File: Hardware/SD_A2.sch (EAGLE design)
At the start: 25 parts, among them IC1 74LS245N, IC2 LM317, IC4 XC9572XL, IC5 28C64ASO

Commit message: Schematic as Eagle V7 file
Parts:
- C2: device rcl:CPOL-EU153CLV-0405 -> rcl@1:CPOL-EU153CLV-0405
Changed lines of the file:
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@@
 <part name="ST1" library="con-apple2" deviceset="A2-50PIN" device="SLOT1-3"/>
 <part name="IC4" library="xilinx-xc9" deviceset="XC9572_S44" device="" value="XC9572XL"/>
-<part name="IC1" library="74xx-eu" library_urn="urn:adsk.eagle:library:85" deviceset="74*245" device="N" technology="LS" value="74LS245N"/>
+<part name="IC1" library="74xx-eu" deviceset="74*245" device="N" technology="LS" value="74LS245N"/>
 <part name="IC2" library="v-reg" deviceset="LM317TL" device="" value="LM317"/>
-<part name="C2" library="rcl" library_urn="urn:adsk.eagle:library:334" deviceset="CPOL-EU" device="153CLV-0405" value="1u"/>
+<part name="C2" library="rcl@1" deviceset="CPOL-EU" device="153CLV-0405" value="1u"/>
 <part name="R1" library="rcl" deviceset="R-EU_" device="R0603" value="200"/>
 <part name="R2" library="rcl" deviceset="R-EU_" device="R0603" value="330"/>
@@
 <part name="GND9" library="supply1" deviceset="GND" device=""/>
 <part name="C1" library="rcl" deviceset="C-EU" device="C0603K" value="100n"/>
-<part name="P+6" library="supply1" library_urn="urn:adsk.eagle:library:371" deviceset="+12V" device=""/>
-<part name="P-1" library="supply1" library_urn="urn:adsk.eagle:library:371" deviceset="-5V" device=""/>
-<part name="P-2" library="supply1" library_urn="urn:adsk.eagle:library:371" deviceset="-12V" device=""/>
-<part name="P+7" library="supply1" library_urn="urn:adsk.eagle:library:371" deviceset="+12V" device=""/>
-<part name="P-3" library="supply1" library_urn="urn:adsk.eagle:library:371" deviceset="-12V" device=""/>
-<part name="P-4" library="supply1" library_urn="urn:adsk.eagle:library:371" deviceset="-5V" device=""/>
+<part name="P+6" library="supply1@1" deviceset="+12V" device=""/>
+<part name="P-1" library="supply1@1" deviceset="-5V" device=""/>
+<part name="P-2" library="supply1@1" deviceset="-12V" device=""/>
+<part name="P+7" library="supply1@1" deviceset="+12V" device=""/>
+<part name="P-3" library="supply1@1" deviceset="-12V" device=""/>
+<part name="P-4" library="supply1@1" deviceset="-5V" device=""/>
 <part name="GND10" library="supply1" deviceset="GND" device=""/>
 <part name="C11" library="rcl" deviceset="C-EU" device="C0603K" value="100n"/>
@@
 <part name="+3V6" library="supply1" deviceset="+3V3" device=""/>
 <part name="GND11" library="supply1" deviceset="GND" device=""/>
-<part name="IC5" library="microchip" library_urn="urn:adsk.eagle:library:294" deviceset="28*64A" device="SO" technology="C"/>
+<part name="IC5" library="microchip" deviceset="28*64A" device="SO" technology="C"/>
 <part name="GND8" library="supply1" deviceset="GND" device=""/>
 <part name="P+5" library="supply1" deviceset="+5V" device=""/>
-<part name="RN1" library="resistor-sil" library_urn="urn:adsk.eagle:library:347" deviceset="GE08R" device="" value="100k"/>
+<part name="RN1" library="resistor-sil" deviceset="GE08R" device="" value="100k"/>
 <part name="+3V3" library="supply1" deviceset="+3V3" device=""/>
 </parts>
@@
 which will not be processed correctly with this version.
 </note>
-<note version="8.2" severity="warning">
-Since Version 8.2, Eagle supports online libraries. The ids
-of those online libraries will not be understood (or retained)
-with this version.
-</note>
 </compatibility>

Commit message: XC9572XL library with VQFP44 package added
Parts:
- IC4: device xilinx-xc9:XC9572_S44 -> xilinx-xc9:XC9572_S44PLCC
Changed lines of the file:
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@@
 <parts>
 <part name="ST1" library="con-apple2" deviceset="A2-50PIN" device="SLOT1-3"/>
-<part name="IC4" library="xilinx-xc9" deviceset="XC9572_S44" device="" value="XC9572XL"/>
+<part name="IC4" library="xilinx-xc9" deviceset="XC9572_S44" device="PLCC" value="XC9572XL"/>
 <part name="IC1" library="74xx-eu" deviceset="74*245" device="N" technology="LS" value="74LS245N"/>
 <part name="IC2" library="v-reg" deviceset="LM317TL" device="" value="LM317"/>

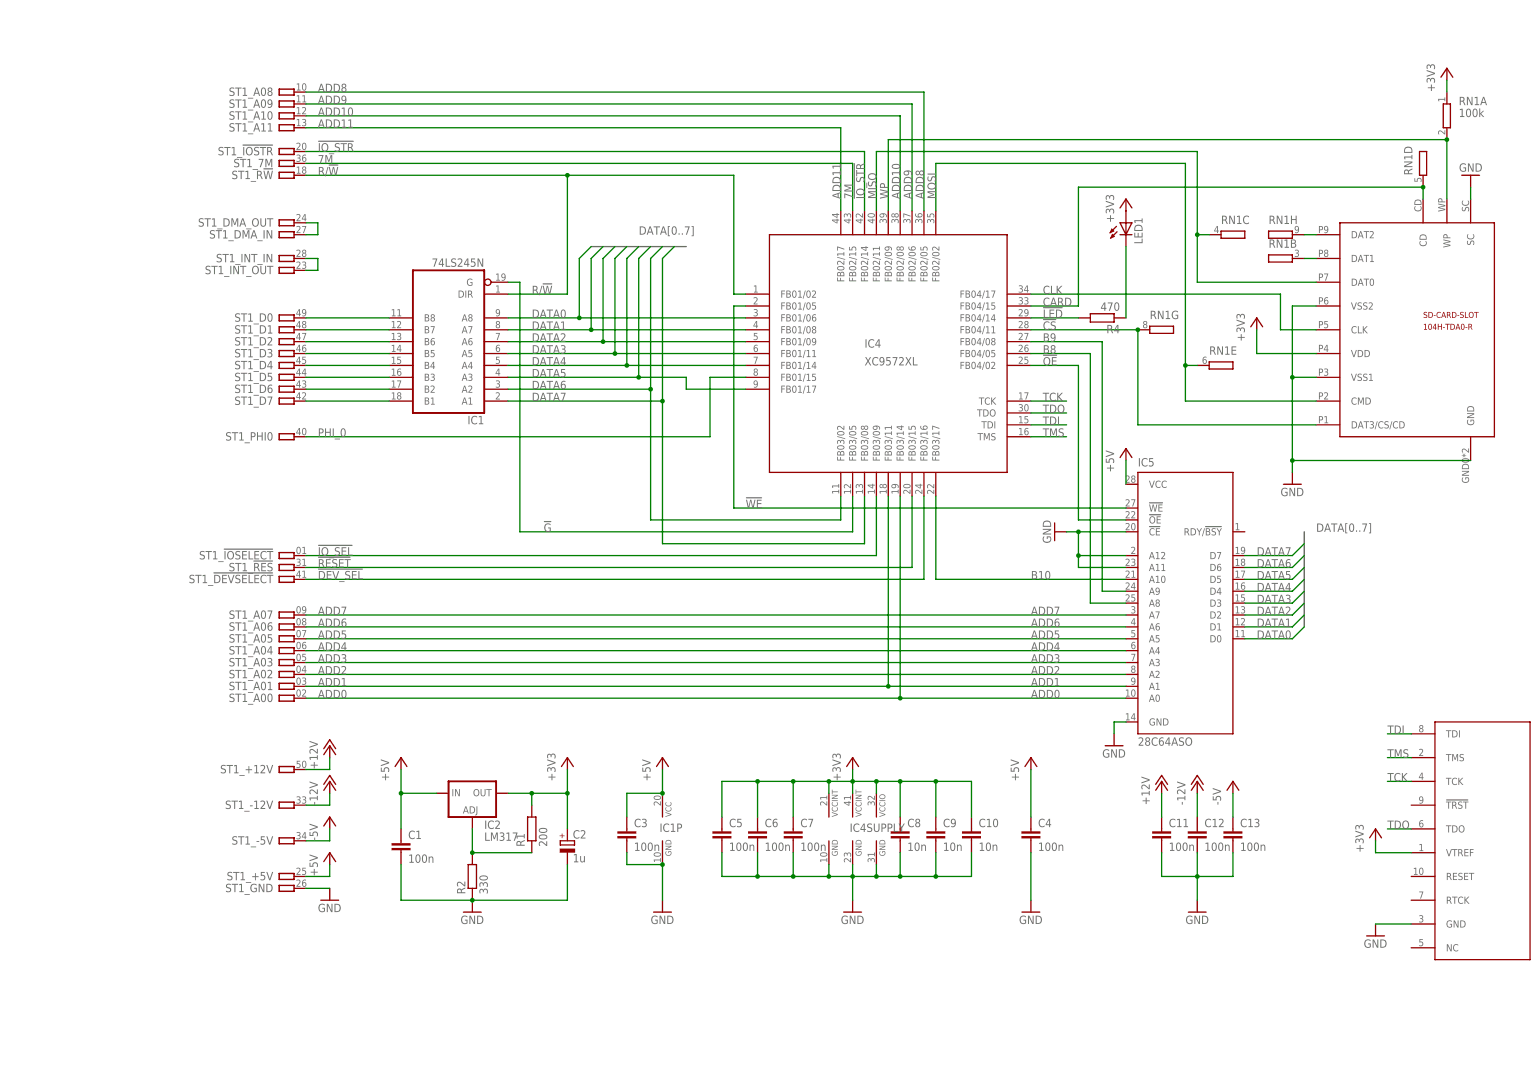
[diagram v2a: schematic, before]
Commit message: CPLD changed to VQFP package
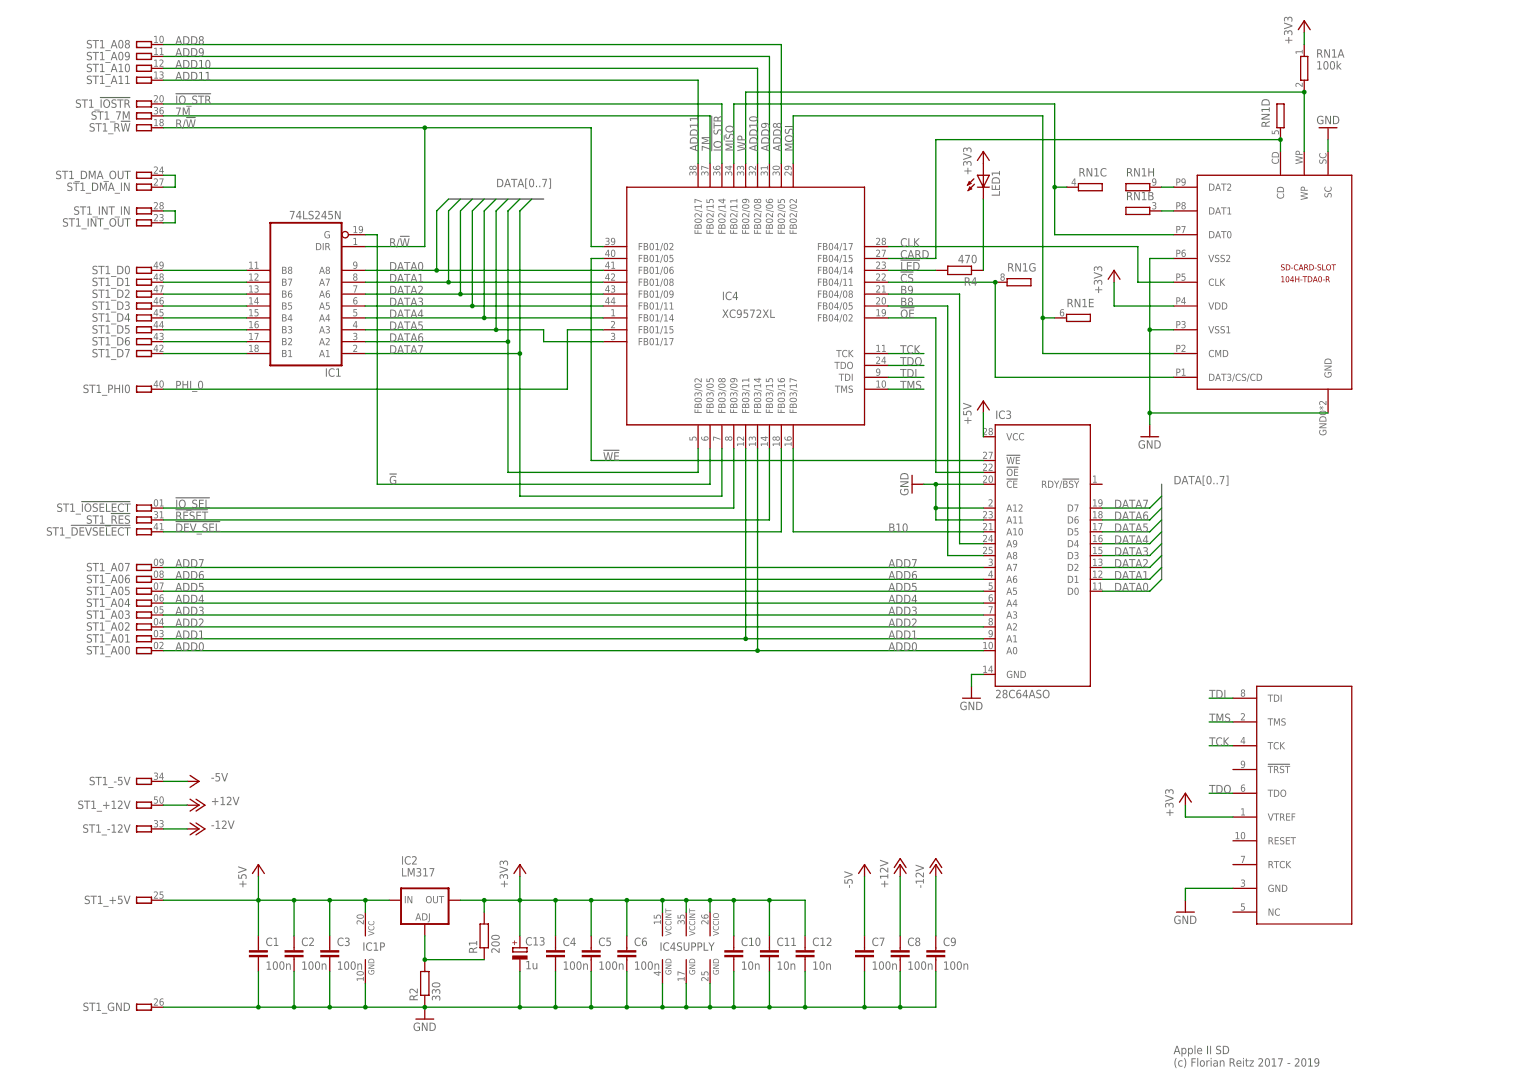
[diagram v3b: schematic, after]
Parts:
- removed IC5: 28C64ASO, microchip:28C64ASO
- added IC3: 28C64ASO, microchip:28C64ASO
- C11, C12: value 100n -> 10n
- C13: value 100n -> 1u; device rcl:C-EUC0603K -> rcl@1:CPOL-EU153CLV-0405
- C2: value 1u -> 100n; device rcl@1:CPOL-EU153CLV-0405 -> rcl:C-EUC0603K
- C8, C9: value 10n -> 100n
- IC4: device xilinx-xc9:XC9572_S44PLCC -> xilinx-xc9:XC9572_S44VQFP
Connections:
- net !OE: now also IC3.!OE; no longer IC5.!OE
- net !WE: now also IC3.!WE; no longer IC5.!WE
- net +12V: now also C8.1; no longer C11.1
- net +3V3: now also C11.1, C12.1, C13.+, C4.1; no longer C2.+, C7.1, C8.1, C9.1
- net +5V: now also C2.1, IC3.VCC; no longer C4.1, IC5.VCC
- net -12V: now also C9.1; no longer C12.1
- net -5V: now also C7.1; no longer C13.1
- net ADD0: now also IC3.A0; no longer IC5.A0
- net ADD1: now also IC3.A1; no longer IC5.A1
- net ADD2: now also IC3.A2; no longer IC5.A2
- net ADD3: now also IC3.A3; no longer IC5.A3
- net ADD4: now also IC3.A4; no longer IC5.A4
- net ADD5: now also IC3.A5; no longer IC5.A5
- net ADD6: now also IC3.A6; no longer IC5.A6
- net ADD7: now also IC3.A7; no longer IC5.A7
- net B10: now also IC3.A10; no longer IC5.A10
- net B8: now also IC3.A8; no longer IC5.A8
- net B9: now also IC3.A9; no longer IC5.A9
- net DATA0: now also IC3.D0; no longer IC5.D0
- net DATA1: now also IC3.D1; no longer IC5.D1
- net DATA2: now also IC3.D2; no longer IC5.D2
- net DATA3: now also IC3.D3; no longer IC5.D3
- net DATA4: now also IC3.D4; no longer IC5.D4
- net DATA5: now also IC3.D5; no longer IC5.D5
- net DATA6: now also IC3.D6; no longer IC5.D6
- net DATA7: now also IC3.D7; no longer IC5.D7
- net GND: now also C13.-, C2.2, IC3.!CE, IC3.A11, IC3.A12, IC3.GND; no longer C13.2, C2.-, IC5.!CE, IC5.A11, IC5.A12, IC5.GND
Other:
- note added: "Apple II SD (c) Florian Reitz 2017 - 2019"
- moved on the sheet: C1, C10, C11, C12, C3, C4, C5, C6, C7, C8, C9, IC1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

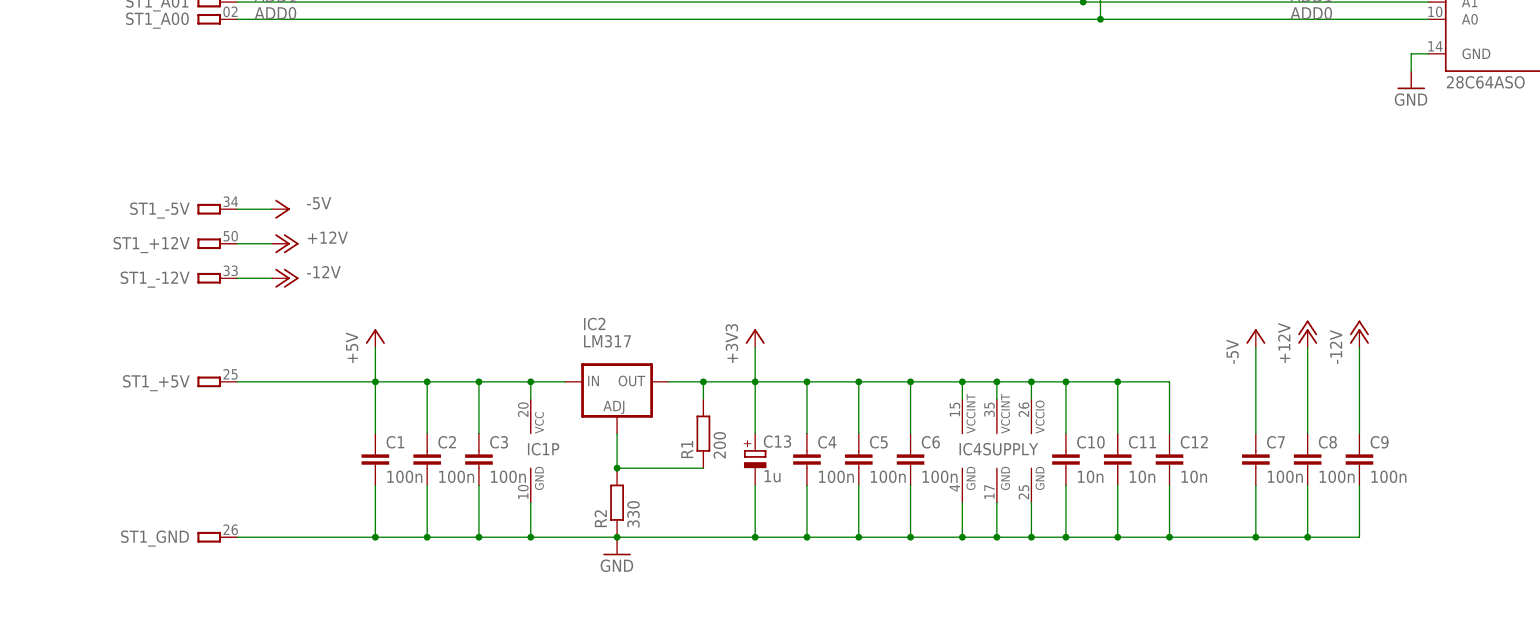
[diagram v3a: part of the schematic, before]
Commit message: LM317 replaced with LM1117
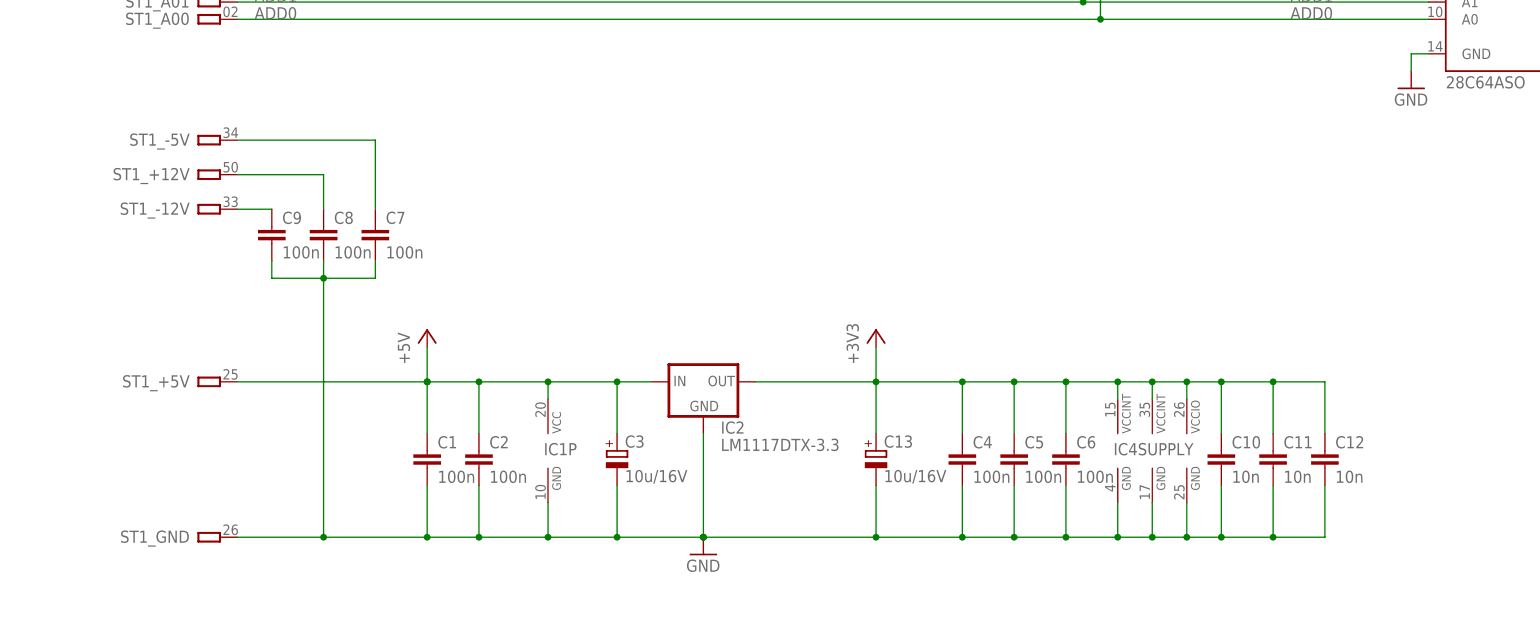
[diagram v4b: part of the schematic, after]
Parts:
- removed R1: 200, rcl:R-EU_R0603
- removed R2: 330, rcl:R-EU_R0603
- C13: value 1u -> 10u/16V; device rcl@1:CPOL-EU153CLV-0405 -> rcl@1:CPOL-EUA/3216-18R
- C3: value 100n -> 10u/16V; device rcl:C-EUC0603K -> rcl@1:CPOL-EUA/3216-18R
- IC2: value LM317 -> LM1117DTX-3.3; device v-reg:LM317TL -> lm1117:LM1117DTX-3.3
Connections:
- removed net N$1: IC2.ADJ, R1.1, R2.2
- net +3V3: no longer R1.2
- net +5V: now also C3.+; no longer C3.1
- net GND: now also C3.-, IC2.GND; no longer C3.2, R2.1
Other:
- moved on the sheet: C1, C10, C11, C12, C13, C2, C4, C5, C6, C7, C8, C9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
